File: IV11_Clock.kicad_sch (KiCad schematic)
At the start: 8 parts, among them J1 DS3231_Conn, J2 PicKit, J3 IV11_Con, U1 PIC16F818-IP

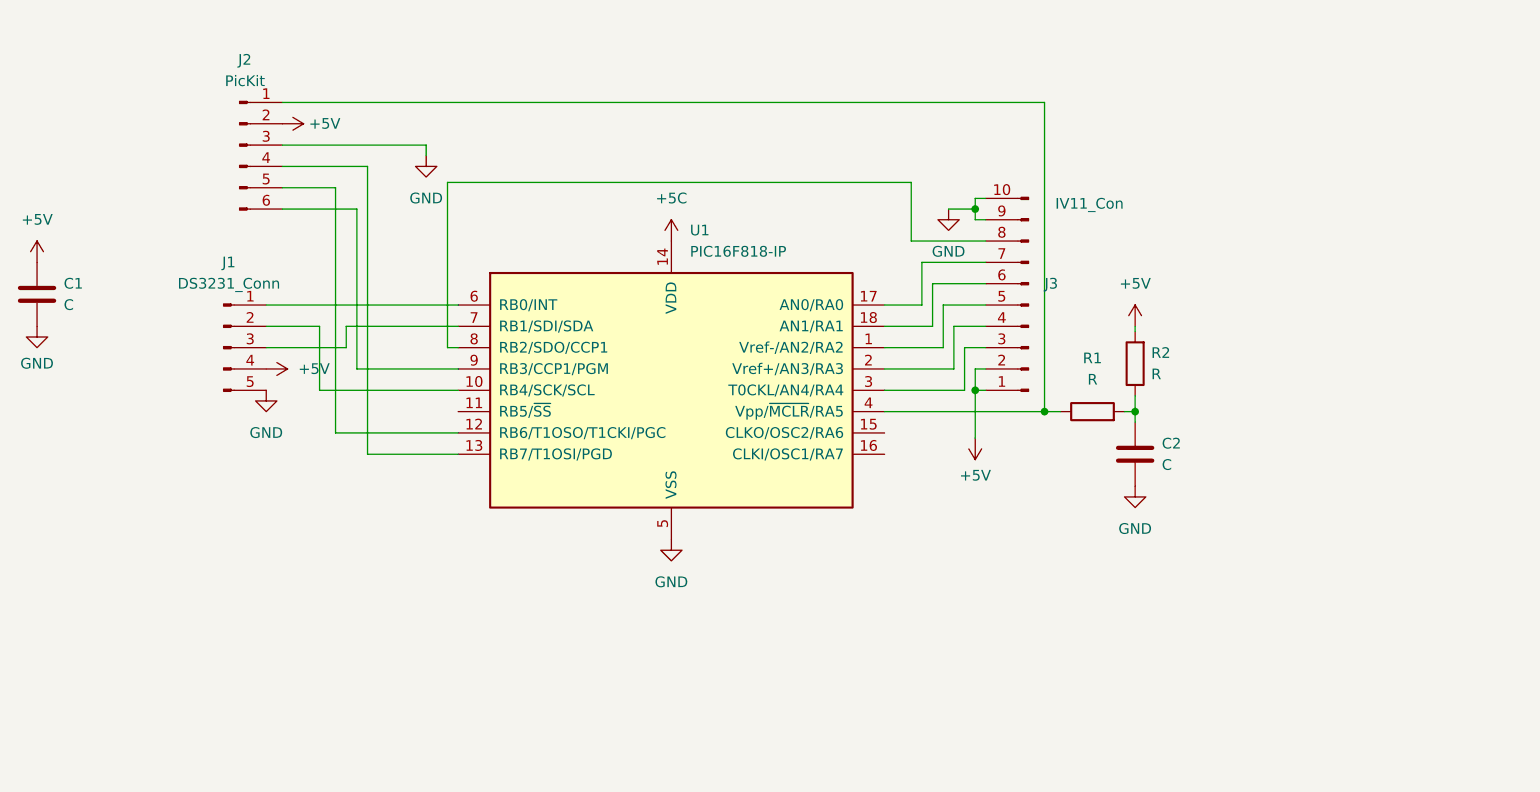
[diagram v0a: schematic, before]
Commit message: Switched to PIC18F26K22
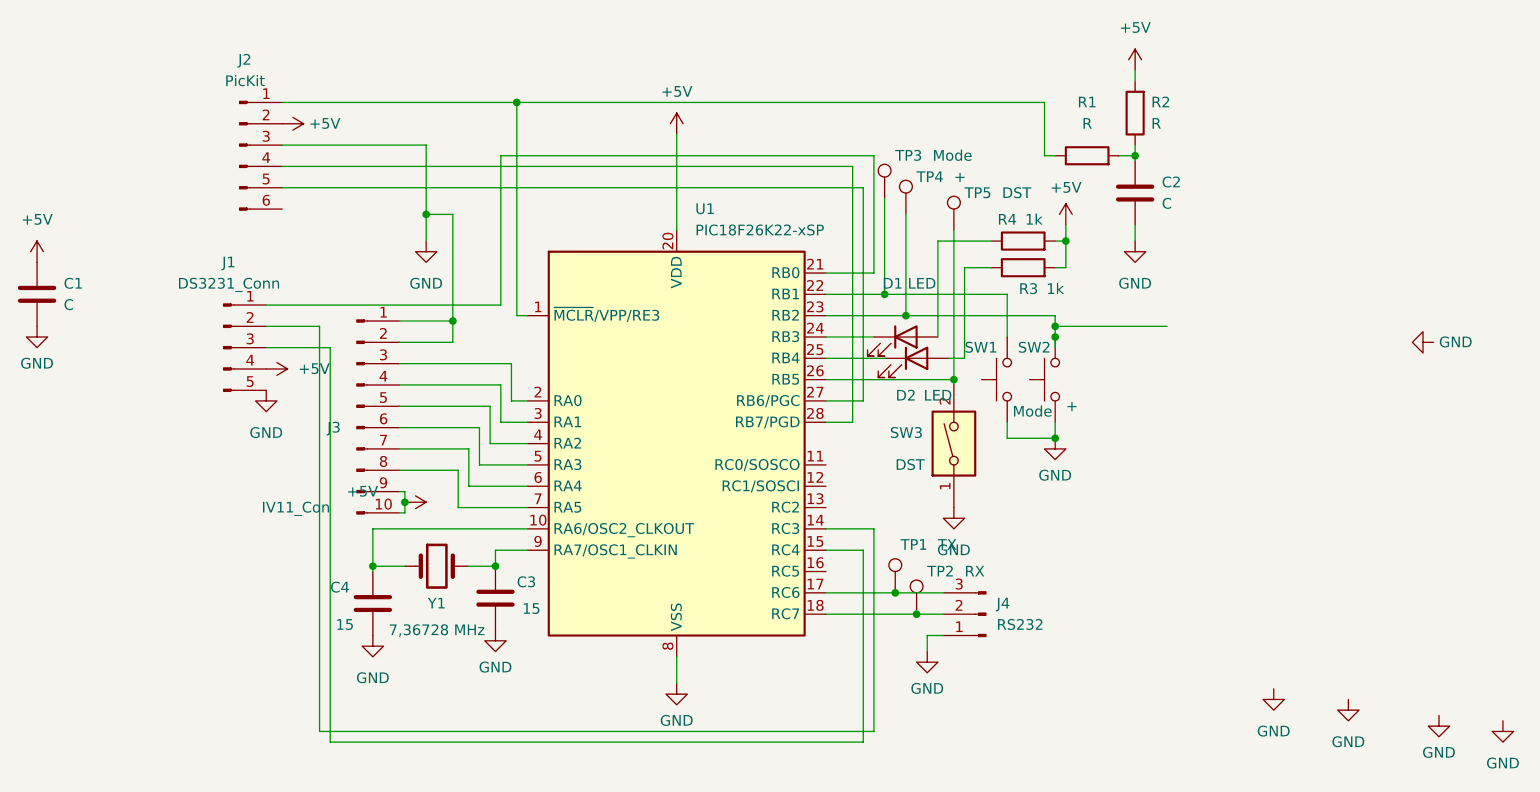
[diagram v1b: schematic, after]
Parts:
- removed U1: PIC16F818-IP, symbol MCU_Microchip_PIC16:PIC16F818-IP
- added C3, C4: 15, Capacitor_SMD:C_0603_1608Metric_Pad1.08x0.95mm_HandSolder, symbol Device:C
- added D1, D2: LED, LED_SMD:LED_0805_2012Metric_Pad1.15x1.40mm_HandSolder, symbol Device:LED
- added J4: RS232, Connector_PinHeader_2.54mm:PinHeader_1x03_P2.54mm_Vertical, symbol Connector:Conn_01x03_Pin
- added R3, R4: 1k, symbol Device:R
- added SW1: Mode, symbol Switch:SW_Push
- added SW2: +, symbol Switch:SW_Push
- added SW3: DST, symbol Switch:SW_DIP_x01
- added TP1: TX, Connector_Pin:Pin_D1.0mm_L10.0mm_LooseFit, symbol Connector:TestPoint
- added TP2: RX, Connector_Pin:Pin_D1.0mm_L10.0mm_LooseFit, symbol Connector:TestPoint
- added TP3: Mode, Connector_Pin:Pin_D1.0mm_L10.0mm_LooseFit, symbol Connector:TestPoint
- added TP4: +, Connector_Pin:Pin_D1.0mm_L10.0mm_LooseFit, symbol Connector:TestPoint
- added TP5: DST, Connector_Pin:Pin_D1.0mm_L10.0mm_LooseFit, symbol Connector:TestPoint
- added U1: PIC18F26K22-xSP, Package_DIP:DIP-28_W7.62mm, symbol MCU_Microchip_PIC18:PIC18F26K22-xSP
- added Y1: 7,36728 MHz, Crystal:Crystal_HC49-U_Vertical, symbol Device:Crystal
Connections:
- net +5V: now also J3.10 (Pin_10), J3.9 (Pin_9), R3.2, R4.2, U1.20 (VDD); no longer J3.1 (Pin_1), J3.2 (Pin_2)
- net GND: now also J3.1 (Pin_1), J3.2 (Pin_2), C3.2, C4.2, J4.1 (Pin_1), SW1.1, SW2.1, SW3.1, U1.19 (VSS), U1.8 (VSS); no longer J3.10 (Pin_10), J3.9 (Pin_9)
- net at J3.5 (Pin_5): now also U1.4 (RA2)
- net at J1.2 (Pin_2): now also U1.14 (RC3)
- net at J2.5 (Pin_5): now also U1.27 (RB6/PGC)
- net at J2.4 (Pin_4): now also U1.28 (RB7/PGD)
- net at J3.7 (Pin_7): now also U1.6 (RA4)
- net at J3.6 (Pin_6): now also U1.5 (RA3)
- net at J3.4 (Pin_4): now also U1.3 (RA1)
- net at J3.3 (Pin_3): now also U1.2 (RA0)
- net at J2.1 (Pin_1), R1.1: now also U1.1 (~{MCLR}/VPP/RE3)
- net at J1.1 (Pin_1): now also U1.21 (RB0)
- net at J1.3 (Pin_3): now also U1.15 (RC4)
- net at J3.8 (Pin_8): now also U1.7 (RA5)
- new net: C3.1, U1.9 (RA7/OSC1_CLKIN), Y1.2
- new net: J4.3 (Pin_3), TP1.1, U1.17 (RC6)
- new net: J4.2 (Pin_2), TP2.1, U1.18 (RC7)
- new net: SW3.2, TP5.1, U1.26 (RB5)
- new net: D1.1 (K), U1.24 (RB3)
- new net: D1.2 (A), R4.1
- new net: C4.1, U1.10 (RA6/OSC2_CLKOUT), Y1.1
- new net: SW1.2, TP3.1, U1.22 (RB1)
- new net: SW2.2, TP4.1, U1.23 (RB2)
- new net: D2.1 (K), U1.25 (RB4)
- new net: D2.2 (A), R3.1
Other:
- moved on the sheet: C2, J3, R1, R2

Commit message: Next
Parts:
- added R5, R6: 33, symbol Device:R
- added TP6: OUT_MS, symbol Connector:TestPoint
- R1: value R -> 1k
- R2: value R -> 20k
- Y1: value 7,36728 MHz -> 7,37628 MHz
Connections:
- net at U1.13 (RC2): now also TP6.1
- net at U1.27 (RB6/PGC): now also R5.2; no longer J2.5 (Pin_5)
- net at U1.28 (RB7/PGD): now also R6.2; no longer J2.4 (Pin_4)
- new net: J2.4 (Pin_4), R6.1
- new net: J2.5 (Pin_5), R5.1
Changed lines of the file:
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@@
+    (stroke (width 0) (type default))
+  )
+  (wire (pts (xy 116.205 71.12) (xy 118.745 71.12))
     (stroke (width 0) (type default))
   )
@@
     (stroke (width 0) (type default))
   )
+  (wire (pts (xy 91.44 33.02) (xy 120.65 33.02))
+    (stroke (width 0) (type default))
+  )
   (wire (pts (xy 116.205 53.34) (xy 123.19 53.34))
     (stroke (width 0) (type default))
@@
     (stroke (width 0) (type default))
   )
-  (wire (pts (xy 51.435 30.48) (xy 119.38 30.48))
-    (stroke (width 0) (type default))
-  )
   (wire (pts (xy 116.205 58.42) (xy 120.65 58.42))
     (stroke (width 0) (type default))
@@
     (stroke (width 0) (type default))
   )
+  (wire (pts (xy 51.435 33.02) (xy 83.82 33.02))
+    (stroke (width 0) (type default))
+  )
   (wire (pts (xy 125.73 48.26) (xy 143.51 48.26))
     (stroke (width 0) (type default))
@@
     (stroke (width 0) (type default))
   )
+  (wire (pts (xy 64.77 30.48) (xy 119.38 30.48))
+    (stroke (width 0) (type default))
+  )
   (wire (pts (xy 116.205 73.66) (xy 121.92 73.66))
     (stroke (width 0) (type default))
@@
     (stroke (width 0) (type default))
   )
+  (wire (pts (xy 51.435 30.48) (xy 57.15 30.48))
+    (stroke (width 0) (type default))
+  )
   (wire (pts (xy 78.74 58.42) (xy 80.645 58.42))
     (stroke (width 0) (type default))
@@
   )
   (wire (pts (xy 55.88 49.53) (xy 49.53 49.53))
-    (stroke (width 0) (type default))
-  )
-  (wire (pts (xy 51.435 33.02) (xy 120.65 33.02))
     (stroke (width 0) (type default))
   )
@@
       (effects (font (size 1.27 1.27)) (justify right))
     )
-    (property "Value" "R" (at 154.94 25.4 0)
+    (property "Value" "20k" (at 154.94 25.4 0)
       (effects (font (size 1.27 1.27)) (justify right))
     )
@@
       (effects (font (size 1.27 1.27)))
     )
-    (property "Value" "R" (at 147.32 25.4 90)
+    (property "Value" "1k" (at 147.32 25.4 90)
       (effects (font (size 1.27 1.27)))
     )
@@
         (path "/1b73cdbb-3aca-458b-970f-3c53a1cdbf67"
           (reference "#PWR05") (unit 1)
+        )
+      )
+    )
+  )
+  (symbol (lib_id "Connector:TestPoint") (at 118.745 71.12 0) (unit 1)
+    (in_bom yes) (on_board yes) (dnp no) (fields_autoplaced)
+    (property "Reference" "TP6" (at 120.65 66.548 0)
+      (effects (font (size 1.27 1.27)) (justify left))
+    )
+    (property "Value" "OUT_MS" (at 120.65 69.088 0)
+      (effects (font (size 1.27 1.27)) (justify left))
+    )
+    (property "Footprint" "" (at 123.825 71.12 0)
+      (effects (font (size 1.27 1.27)) hide)
+    )
+    (property "Datasheet" "~" (at 123.825 71.12 0)
+      (effects (font (size 1.27 1.27)) hide)
+    )
+    (pin "1")
+    (instances
+      (project "IV11_Clock"
+        (path "/1b73cdbb-3aca-458b-970f-3c53a1cdbf67"
+          (reference "TP6") (unit 1)
         )
       )
@@
       (effects (font (size 1.27 1.27)))
     )
-    (property "Value" "7,36728 MHz" (at 69.85 85.725 0)
+    (property "Value" "7,37628 MHz" (at 69.85 85.725 0)
       (effects (font (size 1.27 1.27)))
     )
@@
         )
       )
+    )
+  )
+  (symbol (lib_id "Device:R") (at 60.96 30.48 90) (unit 1)
+    (in_bom yes) (on_board yes) (dnp no)
+    (property "Reference" "R6" (at 62.23 26.67 90)
+      (effects (font (size 1.27 1.27)))
+    )
+    (property "Value" "33" (at 66.04 31.75 90)
+      (effects (font (size 1.27 1.27)))
+    )
+    (property "Footprint" "" (at 60.96 32.258 90)
+      (effects (font (size 1.27 1.27)) hide)
+    )
+    (property "Datasheet" "~" (at 60.96 30.48 0)
+      (effects (font (size 1.27 1.27)) hide)
+    )
+    (pin "1")
+    (pin "2")
+    (instances
+      (project "IV11_Clock"
+        (path "/1b73cdbb-3aca-458b-970f-3c53a1cdbf67"
+          (reference "R6") (unit 1)
+        )
+      )
+    )
+  )
+  (symbol (lib_id "Device:R") (at 87.63 33.02 90) (unit 1)
+    (in_bom yes) (on_board yes) (dnp no)
+    (property "Reference" "R5" (at 92.71 31.75 90)
+      (effects (font (size 1.27 1.27)))
+    )
+    (property "Value" "33" (at 92.075 34.925 90)
+      (effects (font (size 1.27 1.27)))
+    )
+    (property "Footprint" "" (at 87.63 34.798 90)
+      (effects (font (size 1.27 1.27)) hide)
+    )
+    (property "Datasheet" "~" (at 87.63 33.02 0)
+      (effects (font (size 1.27 1.27)) hide)
+    )
+    (pin "1")
+    (pin "2")
+    (instances
+      (project "IV11_Clock"
+        (path "/1b73cdbb-3aca-458b-970f-3c53a1cdbf67"
+          (reference "R5") (unit 1)
+        )
+      )
